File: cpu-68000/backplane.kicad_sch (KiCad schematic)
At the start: 28 parts, among them J201 Conn_03x32_Row_Letter_First, U201 SN74LVCH16T245, U202 SN74LVCH16T245, U203 SN74LXC8T245, U206 SN74LXC8T245

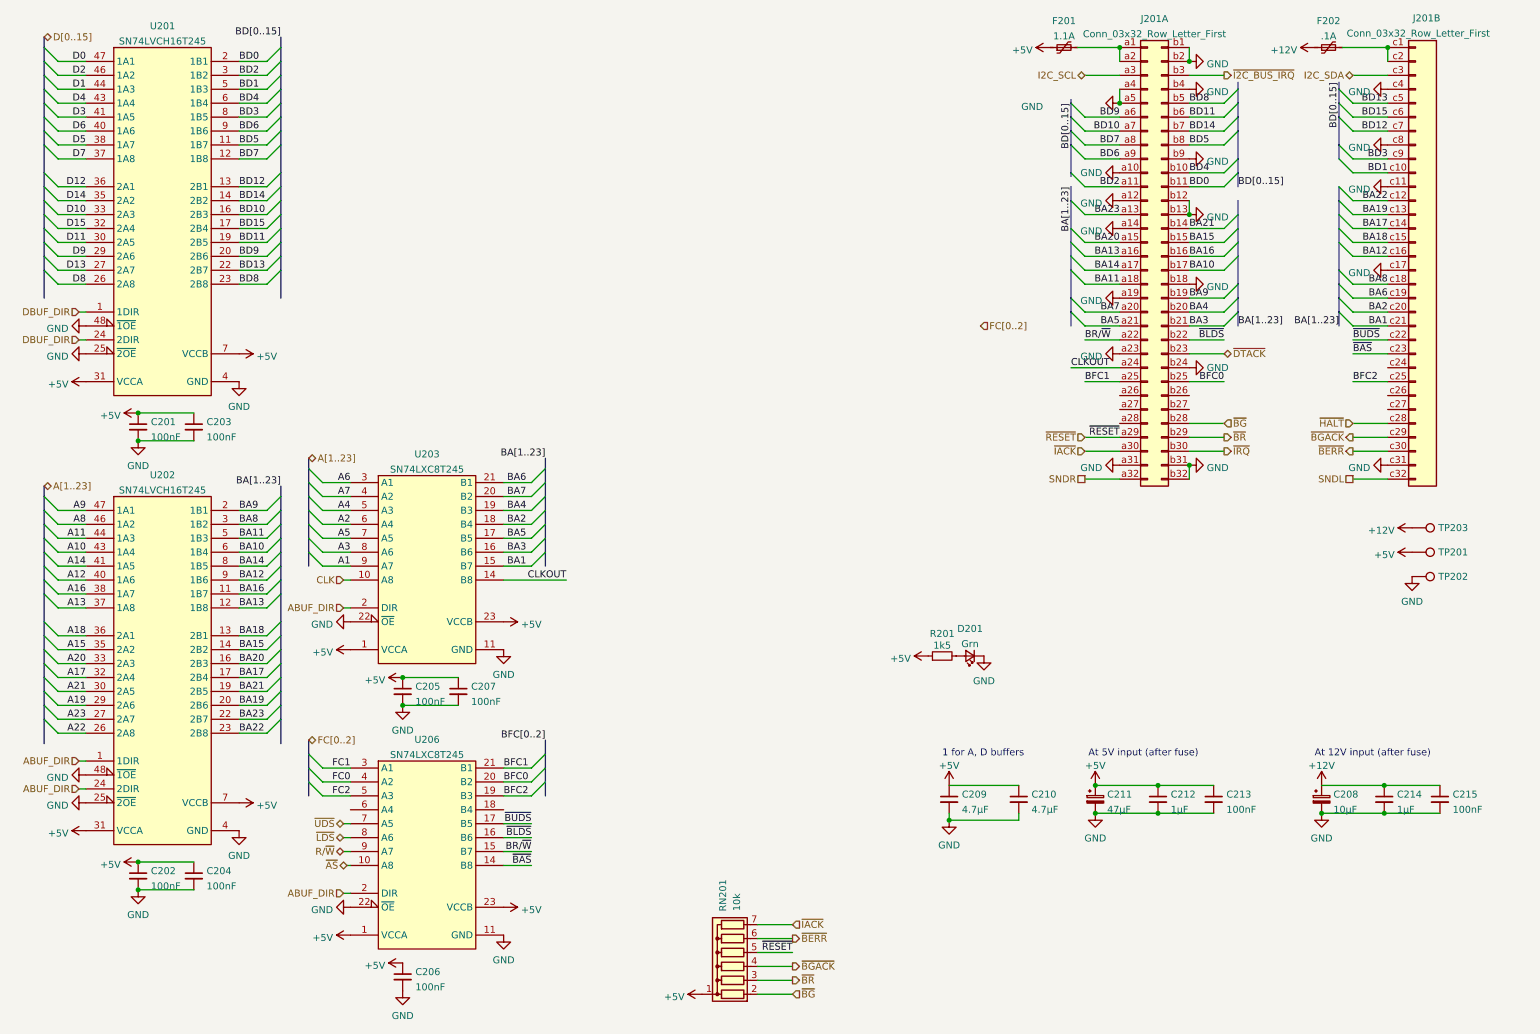
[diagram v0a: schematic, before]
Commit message: Major cleanup of CPU board
- A lot of traces got moved around to be less shitty

- Routed a few more signals to the GALs so that we can eliminate some
  discrete logic, namely for function code checking. This is critical
  since we need to reduce path length when switching the backplane bus
  buffers for each bus transaction as quick as possible.

- Actually provide a clock for the I2C master chip; it shares the clock
  with the audio chips, which is just a bit short of 8MHz.
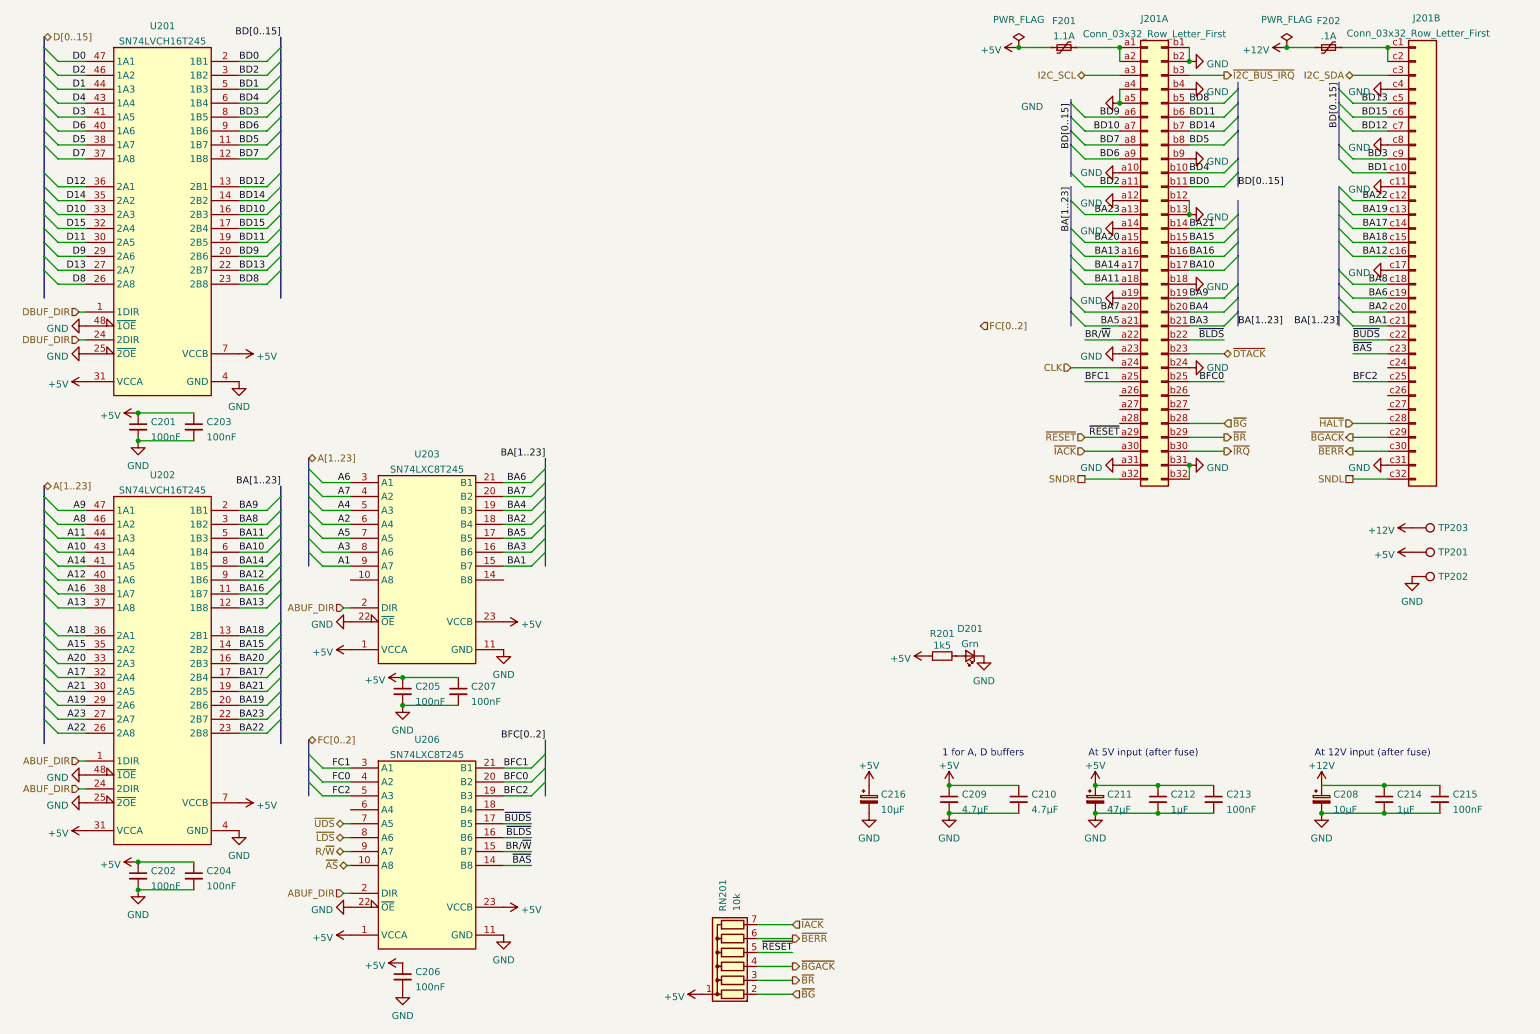
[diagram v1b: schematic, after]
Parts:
- added C216: 10µF, Capacitor_Tantalum_SMD:CP_EIA-3216-18_Kemet-A, symbol Device:C_Polarized_Small
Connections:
- net +5V: now also C216.1
- net CLK: now also J201.a24 (Pin_a24); no longer U203.10 (A8)
- net GND: now also C216.2
- net CLKOUT: no longer names the net of U203.14 (B8)
- net CLKOUT: no longer J201.a24 (Pin_a24)
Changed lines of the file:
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@@
   (junction (at 215.265 19.05) (diameter 0) (color 0 0 0 0)
   )
+  (junction (at 196.85 19.05) (diameter 0) (color 0 0 0 0)
+  )
   (junction (at 215.265 29.21) (diameter 0) (color 0 0 0 0)
   )
@@
   (junction (at 36.195 167.64) (diameter 0) (color 0 0 0 0)
   )
-  (junction (at 184.15 160.02) (diameter 0) (color 0 0 0 0)
+  (junction (at 184.15 153.67) (diameter 0) (color 0 0 0 0)
   )
   (junction (at 252.095 158.75) (diameter 0) (color 0 0 0 0)
@@
   (junction (at 227.965 95.25) (diameter 0) (color 0 0 0 0)
   )
+  (junction (at 184.15 158.75) (diameter 0) (color 0 0 0 0)
+  )
   (junction (at 263.525 158.75) (diameter 0) (color 0 0 0 0)
   )
@@
   (junction (at 222.25 158.75) (diameter 0) (color 0 0 0 0)
   )
+  (junction (at 245.745 19.05) (diameter 0) (color 0 0 0 0)
+  )
   (junction (at 210.82 153.67) (diameter 0) (color 0 0 0 0)
   )
@@
     (stroke (width 0) (type default) (color 0 0 0 0))
   )
-  (wire (pts (xy 102.87 116.205) (xy 114.3 116.205))
-    (stroke (width 0) (type default) (color 0 0 0 0))
-  )
   (bus (pts (xy 110.49 98.425) (xy 110.49 100.965))
     (stroke (width 0) (type default) (color 0 0 0 0))
@@
     (stroke (width 0) (type default) (color 0 0 0 0))
   )
-  (wire (pts (xy 184.15 160.02) (xy 196.85 160.02))
-    (stroke (width 0) (type default) (color 0 0 0 0))
-  )
-  (wire (pts (xy 196.85 160.02) (xy 196.85 158.75))
-    (stroke (width 0) (type default) (color 0 0 0 0))
-  )
-  (wire (pts (xy 184.15 158.75) (xy 184.15 160.02))
+  (wire (pts (xy 184.15 158.75) (xy 196.85 158.75))
     (stroke (width 0) (type default) (color 0 0 0 0))
   )
@@
     (stroke (width 0) (type default) (color 0 0 0 0))
   )
+  (wire (pts (xy 245.745 19.05) (xy 250.825 19.05))
+    (stroke (width 0) (type default) (color 0 0 0 0))
+  )
   (wire (pts (xy 208.915 54.61) (xy 215.265 54.61))
     (stroke (width 0) (type default) (color 0 0 0 0))
@@
     (stroke (width 0) (type default) (color 0 0 0 0))
   )
+  (wire (pts (xy 196.85 19.05) (xy 202.565 19.05))
+    (stroke (width 0) (type default) (color 0 0 0 0))
+  )
   (wire (pts (xy 36.195 85.725) (xy 46.355 85.725))
     (stroke (width 0) (type default) (color 0 0 0 0))
@@
     (stroke (width 0) (type default) (color 0 0 0 0))
   )
-  (wire (pts (xy 73.66 116.205) (xy 74.93 116.205))
-    (stroke (width 0) (type default) (color 0 0 0 0))
-  )
   (wire (pts (xy 54.61 31.75) (xy 59.69 31.75))
     (stroke (width 0) (type default) (color 0 0 0 0))
@@
     (effects (font (size 1.27 1.27)) (justify left bottom))
   )
-  (label "CLKOUT" (at 114.3 116.205 180)
-    (effects (font (size 1.27 1.27)) (justify right bottom))
-  )
   (label "A2" (at 74.93 106.045 180)
     (effects (font (size 1.27 1.27)) (justify right bottom))
@@
     (effects (font (size 1.27 1.27)) (justify right bottom))
   )
-  (label "CLKOUT" (at 206.375 77.47 0)
-    (effects (font (size 1.27 1.27)) (justify left bottom))
-  )
   (label "BA14" (at 54.61 113.665 0)
     (effects (font (size 1.27 1.27)) (justify left bottom))
@@
     (effects (font (size 1.27 1.27)) (justify left))
   )
-  (hierarchical_label "CLK" (shape input) (at 73.66 116.205 180)
+  (hierarchical_label "CLK" (shape input) (at 206.375 77.47 180)
     (effects (font (size 1.27 1.27)) (justify right))
   )
@@
     (pin "b9")
   )
+  (symbol (lib_id "power:PWR_FLAG") (at 245.745 19.05 0) (unit 1)
+    (in_bom yes) (on_board yes) (fields_autoplaced)
+    (property "Reference" "#FLG0102" (id 0) (at 245.745 17.145 0)
+      (effects (font (size 1.27 1.27)) hide)
+    )
+    (property "Value" "PWR_FLAG" (id 1) (at 245.745 13.97 0))
+    (property "Footprint" "" (id 2) (at 245.745 19.05 0)
+      (effects (font (size 1.27 1.27)) hide)
+    )
+    (property "Datasheet" "~" (id 3) (at 245.745 19.05 0)
+      (effects (font (size 1.27 1.27)) hide)
+    )
+    (pin "1")
+  )
+  (symbol (lib_id "power:+5V") (at 169.545 153.67 0) (unit 1)
+    (in_bom yes) (on_board yes) (fields_autoplaced)
+    (property "Reference" "#PWR0236" (id 0) (at 169.545 157.48 0)
+      (effects (font (size 1.27 1.27)) hide)
+    )
+    (property "Value" "+5V" (id 1) (at 169.545 150.0655 0))
+    (property "Footprint" "" (id 2) (at 169.545 153.67 0)
+      (effects (font (size 1.27 1.27)) hide)
+    )
+    (property "Datasheet" "" (id 3) (at 169.545 153.67 0)
+      (effects (font (size 1.27 1.27)) hide)
+    )
+    (pin "1")
+  )
   (symbol (lib_id "power:GND") (at 215.265 74.93 270) (unit 1)
     (in_bom yes) (on_board yes) (fields_autoplaced)
@@
     (pin "9")
   )
-  (symbol (lib_id "power:+12V") (at 250.825 19.05 90) (unit 1)
+  (symbol (lib_id "power:+12V") (at 245.745 19.05 90) (unit 1)
     (in_bom yes) (on_board yes) (fields_autoplaced)
-    (property "Reference" "#PWR0264" (id 0) (at 254.635 19.05 0)
+    (property "Reference" "#PWR0264" (id 0) (at 249.555 19.05 0)
       (effects (font (size 1.27 1.27)) hide)
     )
-    (property "Value" "+12V" (id 1) (at 247.65 19.529 90)
+    (property "Value" "+12V" (id 1) (at 242.57 19.529 90)
       (effects (font (size 1.27 1.27)) (justify left))
     )
-    (property "Footprint" "" (id 2) (at 250.825 19.05 0)
+    (property "Footprint" "" (id 2) (at 245.745 19.05 0)
       (effects (font (size 1.27 1.27)) hide)
     )
-    (property "Datasheet" "" (id 3) (at 250.825 19.05 0)
+    (property "Datasheet" "" (id 3) (at 245.745 19.05 0)
       (effects (font (size 1.27 1.27)) hide)
     )
@@
     (pin "2")
   )
-  (symbol (lib_id "power:+5V") (at 202.565 19.05 90) (unit 1)
+  (symbol (lib_id "power:+5V") (at 196.85 19.05 90) (unit 1)
     (in_bom yes) (on_board yes) (fields_autoplaced)
-    (property "Reference" "#PWR0249" (id 0) (at 206.375 19.05 0)
+    (property "Reference" "#PWR0249" (id 0) (at 200.66 19.05 0)
       (effects (font (size 1.27 1.27)) hide)
     )
-    (property "Value" "+5V" (id 1) (at 199.39 19.529 90)
+    (property "Value" "+5V" (id 1) (at 193.675 19.529 90)
       (effects (font (size 1.27 1.27)) (justify left))
     )
-    (property "Footprint" "" (id 2) (at 202.565 19.05 0)
+    (property "Footprint" "" (id 2) (at 196.85 19.05 0)
       (effects (font (size 1.27 1.27)) hide)
     )
-    (property "Datasheet" "" (id 3) (at 202.565 19.05 0)
+    (property "Datasheet" "" (id 3) (at 196.85 19.05 0)
       (effects (font (size 1.27 1.27)) hide)
     )
@@
     (pin "1")
   )
-  (symbol (lib_id "power:GND") (at 184.15 160.02 0) (unit 1)
+  (symbol (lib_id "power:GND") (at 184.15 158.75 0) (unit 1)
     (in_bom yes) (on_board yes) (fields_autoplaced)
-    (property "Reference" "#PWR0151" (id 0) (at 184.15 166.37 0)
+    (property "Reference" "#PWR0151" (id 0) (at 184.15 165.1 0)
       (effects (font (size 1.27 1.27)) hide)
     )
-    (property "Value" "GND" (id 1) (at 184.15 164.5824 0))
-    (property "Footprint" "" (id 2) (at 184.15 160.02 0)
+    (property "Value" "GND" (id 1) (at 184.15 163.3124 0))
+    (property "Footprint" "" (id 2) (at 184.15 158.75 0)
       (effects (font (size 1.27 1.27)) hide)
     )
-    (property "Datasheet" "" (id 3) (at 184.15 160.02 0)
+    (property "Datasheet" "" (id 3) (at 184.15 158.75 0)
       (effects (font (size 1.27 1.27)) hide)
     )
@@
     (pin "1")
   )
+  (symbol (lib_id "power:GND") (at 169.545 158.75 0) (unit 1)
+    (in_bom yes) (on_board yes) (fields_autoplaced)
+    (property "Reference" "#PWR0238" (id 0) (at 169.545 165.1 0)
+      (effects (font (size 1.27 1.27)) hide)
+    )
+    (property "Value" "GND" (id 1) (at 169.545 163.3124 0))
+    (property "Footprint" "" (id 2) (at 169.545 158.75 0)
+      (effects (font (size 1.27 1.27)) hide)
+    )
+    (property "Datasheet" "" (id 3) (at 169.545 158.75 0)
+      (effects (font (size 1.27 1.27)) hide)
+    )
+    (pin "1")
+  )
   (symbol (lib_id "power:GND") (at 210.82 158.75 0) (unit 1)
     (in_bom yes) (on_board yes) (fields_autoplaced)
@@
     (pin "2")
   )
+  (symbol (lib_id "Device:C_Polarized_Small") (at 169.545 156.21 0) (unit 1)
+    (in_bom yes) (on_board yes) (fields_autoplaced)
+    (property "Reference" "C216" (id 0) (at 171.704 155.3015 0)
+      (effects (font (size 1.27 1.27)) (justify left))
+    )
+    (property "Value" "10µF" (id 1) (at 171.704 158.0766 0)
+      (effects (font (size 1.27 1.27)) (justify left))
+    )
+    (property "Footprint" "Capacitor_Tantalum_SMD:CP_EIA-3216-18_Kemet-A" (id 2) (at 169.545 156.21 0)
+      (effects (font (size 1.27 1.27)) hide)
+    )
+    (property "Datasheet" "~" (id 3) (at 169.545 156.21 0)
+      (effects (font (size 1.27 1.27)) hide)
+    )
+    (pin "1")
+    (pin "2")
+  )
   (symbol (lib_id "power:GND") (at 215.265 46.99 270) (unit 1)
     (in_bom yes) (on_board yes) (fields_autoplaced)
@@
       (effects (font (size 1.27 1.27)) hide)
     )
+    (pin "1")
+  )
+  (symbol (lib_id "power:PWR_FLAG") (at 196.85 19.05 0) (unit 1)
+    (in_bom yes) (on_board yes) (fields_autoplaced)
+    (property "Reference" "#FLG0101" (id 0) (at 196.85 17.145 0)
+      (effects (font (size 1.27 1.27)) hide)
+    )
+    (property "Value" "PWR_FLAG" (id 1) (at 196.85 13.97 0))
+    (property "Footprint" "" (id 2) (at 196.85 19.05 0)
+      (effects (font (size 1.27 1.27)) hide)
+    )
+    (property "Datasheet" "~" (id 3) (at 196.85 19.05 0)
+      (effects (font (size 1.27 1.27)) hide)
+    )
